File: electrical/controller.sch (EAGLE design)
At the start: 39 parts, among them IC1 555, IC2 MCP4728, J3 455-1750-1-ND, Q1 DMP3098, Q2 DMG3402L-7, Q3 600mA/40V, Q4 DMP3098, U1 U3V16F15, U2 U3V16F15, U5 MCP6042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

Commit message: Add 555 Restart into the integrated code
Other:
- note added: "TIMER_RESTART will go HIGH after 1M * 4.7uF = 4.7 sec of no pulses."
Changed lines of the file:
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@@
 As comparator to DAC voltage
 To trigger @ zero crossing.</text>
+<text x="7.62" y="43.18" size="1.27" layer="91">TIMER_RESTART will go HIGH after
+1M * 4.7uF = 4.7 sec of no pulses.</text>
 </plain>
 <instances>

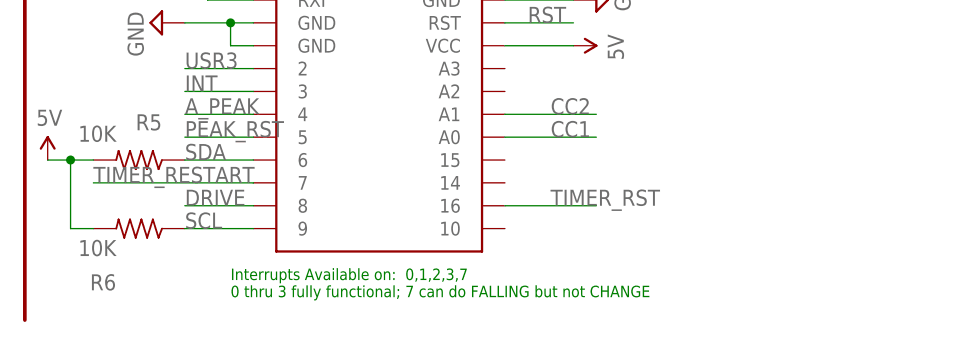
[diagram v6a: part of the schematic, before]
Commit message: Add more power, duration tests.
Turns out that the Low Power library's durations aren't precise -
they're approximate.

The only way to do precise powerdowns seems to be by leveraging Timer1 /
Timer3 calling some interrupt as a way to get us out of the Idle mode.
Works only for IDLE.

Thus -->
Precise timing less than 8.3 seconds: use timer_sleep (17.1 ma)

Imprecise timing with less wake up time: use powerStandby (560 uA)
Imprecise timing with more wake p time: use powerDown (70uA)

powerDown vs powerSave doesnt really matter for me - there is no Timer2
on the APM that we can use.
See section 7.6 on the ATMEGA 32u4 datasheet:
https://ww1.microchip.com/downloads/en/devicedoc/atmel-7766-8-bit-avr-atmega16u4-32u4_datasheet.pdf

I will go and try:
PowerStandby
and
BOD

Standby keeps the crystal on but turns more things off, so, it may be a
good idea...
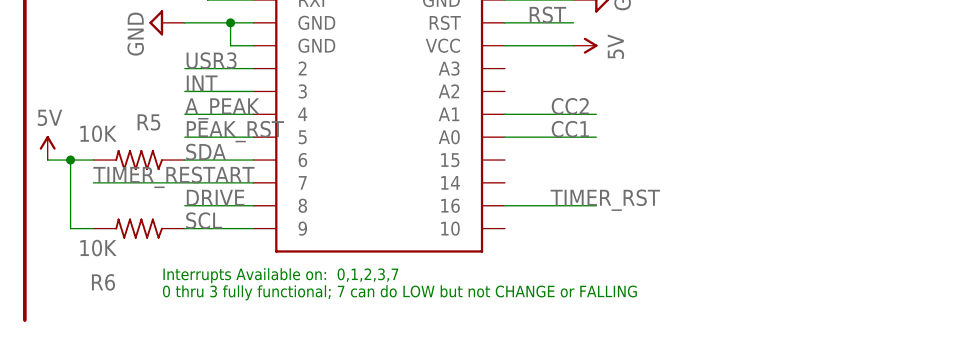
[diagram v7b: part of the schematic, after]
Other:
- note added: "Interrupts Available on: 0,1,2,3,7 0 thru 3 fully functional; 7 can do LOW but not CHANGE or FALLING"
- note removed: "Interrupts Available on: 0,1,2,3,7 0 thru 3 fully functional; 7 can do FALLING but not CHANGE"
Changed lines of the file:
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@@
 <wire x1="91.44" y1="55.88" x2="170.18" y2="55.88" width="0.4064" layer="94"/>
 <text x="213.36" y="48.26" size="5.08" layer="97">Mounting</text>
-<text x="96.52" y="2.54" size="1.27" layer="91">Interrupts Available on:  0,1,2,3,7
-0 thru 3 fully functional; 7 can do FALLING but not CHANGE</text>
+<text x="88.9" y="2.54" size="1.27" layer="91">Interrupts Available on:  0,1,2,3,7
+0 thru 3 fully functional; 7 can do LOW but not CHANGE or FALLING</text>
 <text x="127" y="40.64" size="1.27" layer="91">The scoop on the pinout:
 - hardware i2c is 2/3: those are taken by interrupts.

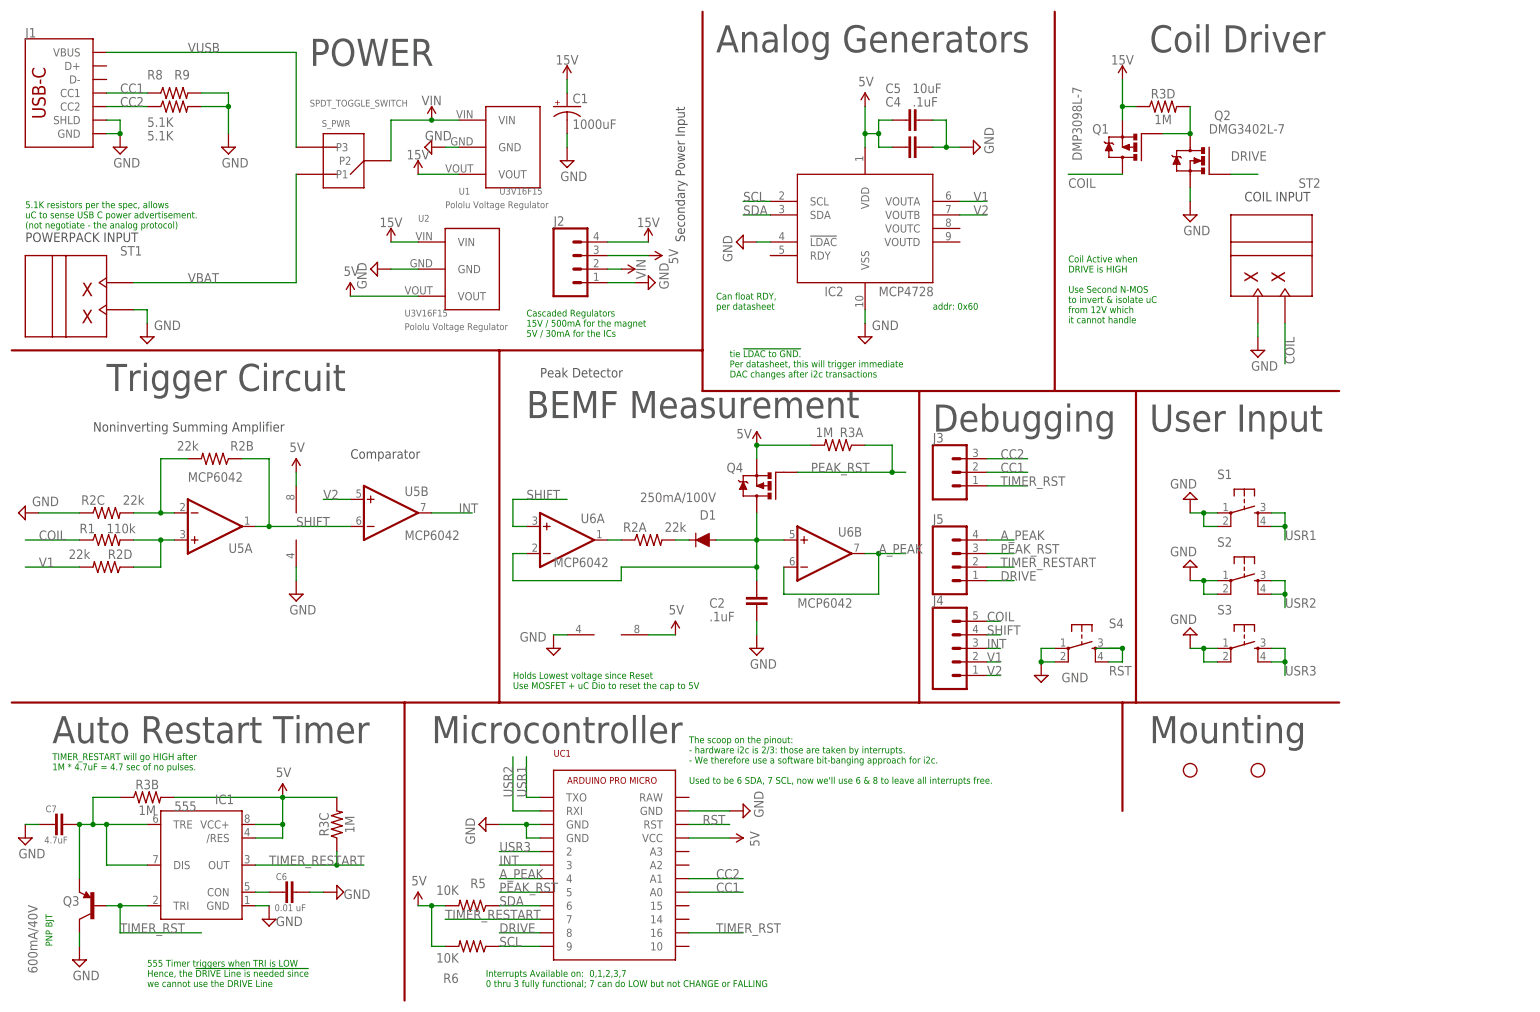
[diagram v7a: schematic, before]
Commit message: Massive SCH changes for Rev D3
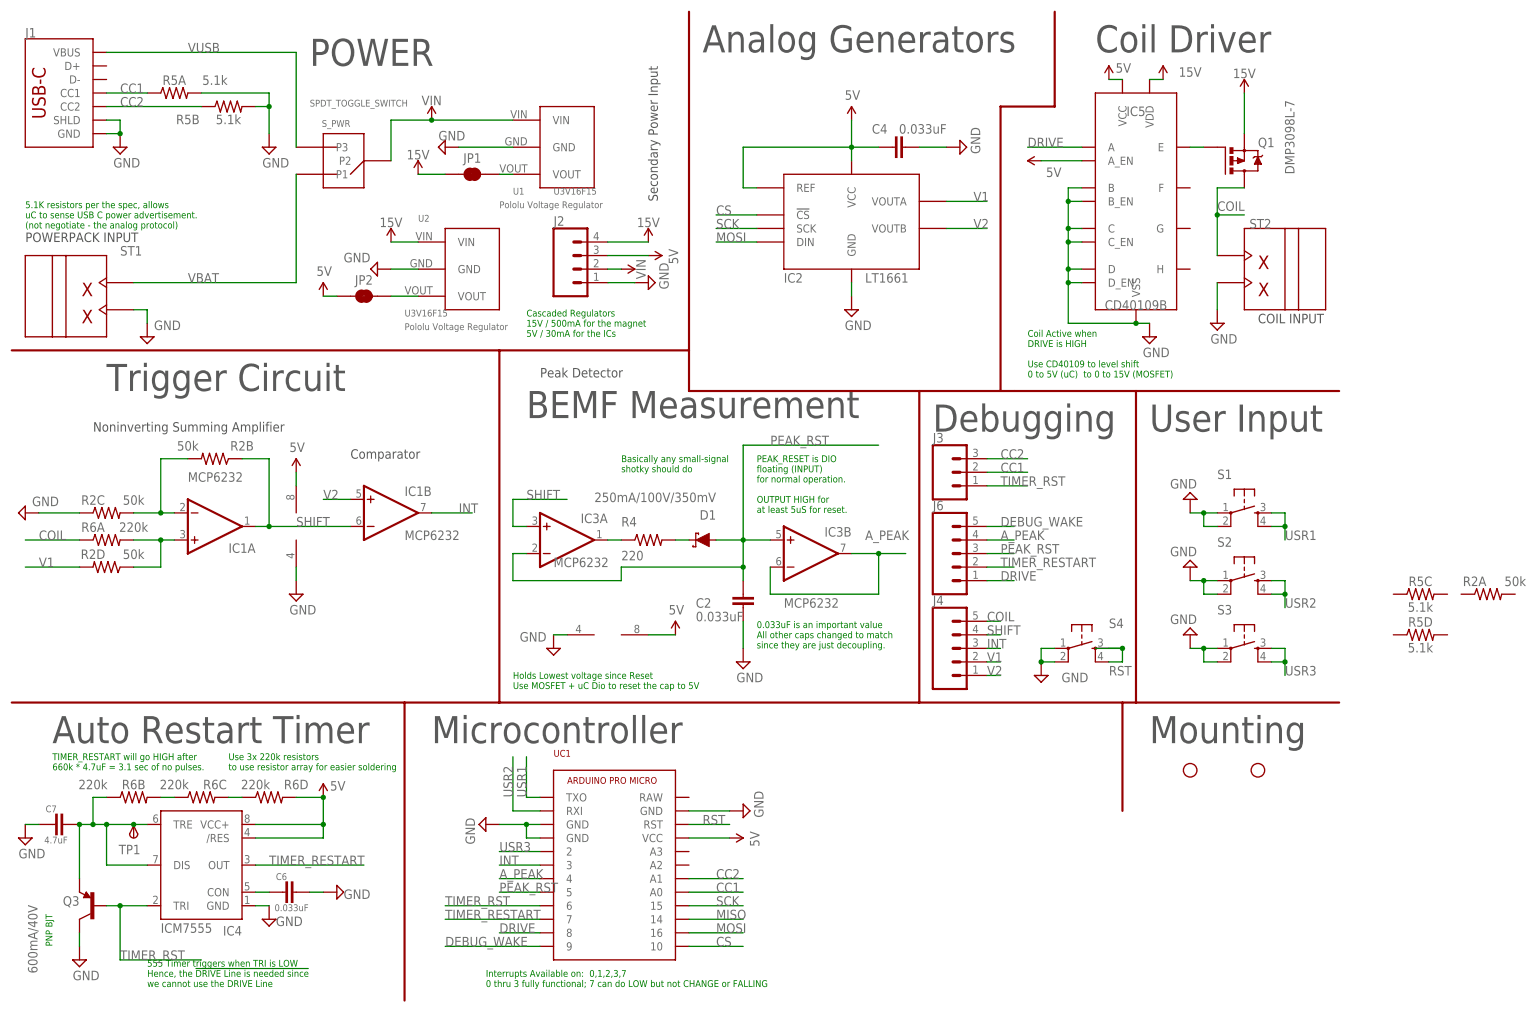
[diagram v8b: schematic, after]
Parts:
- removed C1: 1000uF, SparkFun-Capacitors:CAP_POLPTH4
- removed C5: 10uF, pie:CAP0805
- removed J5: (no value), SparkFun-Connectors:CONN_04PTH
- removed Q2: DMG3402L-7, BEST_Custom:N-CHANNEL-MOSFETSOT23-3
- removed Q4: DMP3098, BEST_Custom:P-CHANNEL-MOSFETSOT23-3
- removed R1: 110k, pie:R-US_R0603
- removed R3: 1M, BEST_Custom:RESISTOR_ARRAY_(4)-2012-1/8W-5%
- removed R8, R9: 5.1K, pie:R-US_R0603
- removed U5: MCP6042, BEST_Custom:MCP602SN
- added IC4: ICM7555, SparkFun-IC-Special-Function:555D
- added IC5: CD40109B, BEST_Custom:CD40109BTSSOP16
- added J6: (no value), SparkFun-Connectors:CONN_05PTH
- added JP1, JP2: JUMPER-SMT_2_NC_TRACE_SILK, SparkFun-Jumpers:JUMPER-SMT_2_NC_TRACE_SILK
- added R4: 220, BEST_Custom:R-US_R0603
- added TP1: TPSPAD1-13, testpad:TPSPAD1-13
- C2, C4: value .1uF -> 0.033uF
- C6: value 0.01 uF -> 0.033uF
- D1: value 250mA/100V -> 250mA/100V/350mV; device SparkFun-DiscreteSemi:DIODE-BAS16J -> SparkFun-DiscreteSemi:DIODE-SCHOTTKY-BAT60A
- IC1: value 555 -> MCP6232; device SparkFun-IC-Special-Function:555D -> BEST_Custom:MCP602SN
- IC2: value MCP4728 -> LTC1661MSOP8; device BEST_Custom:MCP4728 -> BEST_Custom:LTC1661MSOP8
- IC3: value MCP6042 -> MCP6232
- R2: value 22k -> 50k; device BEST_Custom:RESISTOR_ARRAY_(4)-2012-1/8W-5% -> BEST_Custom:RESISTOR_ARRAY_(4)-1206-1/16W-5%
- R5: value 10K -> 5.1k; device pie:R-US_R0603 -> BEST_Custom:RESISTOR_ARRAY_(4)-1206-1/16W-5%
- R6: value 10K -> 220k; device pie:R-US_R0603 -> BEST_Custom:RESISTOR_ARRAY_(4)-1206-1/16W-5%
- renumbered U6 to IC3
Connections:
- removed net SCL: IC2.SCL, R6.1, UC1.9
- removed net SDA: IC2.SDA, R5.1, UC1.6
- new net 12V: IC5.VDD, JP1.1
- new net CS: IC2.!CS, UC1.10
- new net DEBUG_WAKE: J6.5, UC1.9
- new net MISO: UC1.14
- new net MOSI: IC2.DIN, UC1.16
- new net N$10: R6C.2, R6D.1
- new net N$11: IC5.E, Q1.G
- new net N$8: JP1.2, U1.VOUT
- new net N$9: JP2.2, U2.VOUT
- new net SCK: IC2.SCK, UC1.15
- net 15V: no longer C1.+, R3D.1, U1.VOUT
- net 5V: now also IC1P.V+, IC2.REF, IC2.VCC, IC4./RES, IC4.VCC+, IC5.A_EN, IC5.VCC, JP2.1, R6D.2; no longer C5.1, IC1./RES, IC1.VCC+, IC2.VDD, Q4.S, R3A.2, R3B.2, R3C.2, R5.2, R6.2, U2.VOUT, U5P.V+
- net A_PEAK: now also J6.4; no longer J5.4
- net CC1: now also R5A.1; no longer R8.1
- net CC2: now also R5B.1; no longer R9.1
- net COIL: now also R6A.1; no longer R1.1
- net DRIVE: now also IC5.A, J6.1; no longer J5.1, Q1.G, Q2.D, Q2.G, R3D.2
- net GND: now also IC1P.V-, IC2.GND, IC4.GND, IC5.B, IC5.B_EN, IC5.C, IC5.C_EN, IC5.D, IC5.D_EN, IC5.VSS, R5A.2, R5B.2; no longer C1.-, C5.2, IC1.GND, IC2.!LDAC, IC2.VSS, Q2.S@2, R8.2, R9.2, U5P.V-
- net INT: now also IC1B.OUT; no longer U5B.OUT
- net N$1: now also D1.C, R4.2; no longer C2.1, D1.A, IC3A.-IN, IC3B.+IN, Q4.D
- net N$2: now also R4.1; no longer R2A.1
- net N$3: now also R6B.2, R6C.1; no longer D1.C, R2A.2
- net N$4: now also IC1A.+IN, R6A.2; no longer R1.2, U5A.+IN
- net N$5: now also IC1A.-IN; no longer U5A.-IN
- net N$6: now also IC4.CON; no longer IC1.CON
- net N$7: now also IC4.DIS, IC4.TRE, R6B.1, TP1.PP; no longer IC1.DIS, IC1.TRE, R3B.1
- net PEAK_RST: now also C2.1, D1.A, IC3A.-IN, IC3B.+IN, J6.3; no longer J5.3, Q4.G, R3A.1
- net SHIFT: now also IC1A.OUT, IC1B.-IN; no longer U5A.OUT, U5B.-IN
- net TIMER_RESTART: now also IC4.OUT, J6.2; no longer IC1.OUT, J5.2, R3C.1
- net TIMER_RST: now also IC4.TRI, UC1.6; no longer IC1.TRI, UC1.16
- net V2: now also IC1B.+IN; no longer U5B.+IN
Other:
- note added: "0.033uF is an important value All other caps changed to match since they are just decoupling."
- note added: "Basically any small-signal shotky should do"
- note added: "Coil Active when DRIVE is HIGH Use CD40109 to level shift 0 to 5V (uC) to 0 to 15V (MOSFET)"
- note added: "PEAK_RESET is DIO floating (INPUT) for normal operation. OUTPUT HIGH for at least 5uS for reset."
- note added: "Previous 5V coil operation chose Coil = 1, V+ = 1.5, all resistors 10k. 2.69 b/c the new coil has 2.69 the turns of the old one."
- note added: "Stage 1: V+ = (R1*V1 + R2*Vcoil) / (R1 + R2) Solve for Values by solving simultaneous equations: 1) Set Coil = 0, choose V+ = 1V (VShift = 2V) 2) Set Coil = 2.69, choose V+ = 1.5V (VShift = 3V) Solve simultaneously to find that R1 = 4.38 R2. Choose R2 = 220 (for part unification) R1 = 50.22k (choose 50k)"
- note added: "TIMER_RESTART will go HIGH after 660k * 4.7uF = 3.1 sec of no pulses."
- note added: "Use 3x 220k resistors to use resistor array for easier soldering"
- note removed: "Can float RDY, per datasheet"
- note removed: "Coil Active when DRIVE is HIGH Use Second N-MOS to invert & isolate uC from 12V which it cannot handle"
- note removed: "Stage 1: V+ = R1*V1 + R2*Vcoil / (R1 + R2) Choose R2 = 22k. (For part unification) Solve for Values by solving simultaneous equations: 1) Set Coil = 0, choose V+ = 1V ==> VShift = 2V 2) Set Coil = 3, choose V+ = 1.5V ==> VShift = 3V Previous 5V coil operation chose Coil = 1, V+ = 1.5 (approx 3x the coil count, 1/3 the gain), all resistors 10k. (Actually it's 2.69x the coil count, todo adjust late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"
- note removed: "TIMER_RESTART will go HIGH after 1M * 4.7uF = 4.7 sec of no pulses."
- note removed: "The scoop on the pinout: - hardware i2c is 2/3: those are taken by interrupts. - We therefore use a software bit-banging approach for i2c. Used to be 6 SDA, 7 SCL, now we'll use 6 & 8 to leave all interrupts free."
- note removed: "addr: 0x60"
- note removed: "tie !LDAC to GND. Per datasheet, this will trigger immediate DAC changes after i2c transactions"
- moved on the sheet: C2, C4, Q1, R2A, ST2, U1
